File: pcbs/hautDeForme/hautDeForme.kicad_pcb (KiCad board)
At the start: 2 copper layers, 29.8 x 68.3 mm, 40 parts, among them J1 Conn_02x07_Counter_Clockwise, J6 USB4105-GF-A, U2 AZ1117CH-3.3TRG1, U4 CP2102N

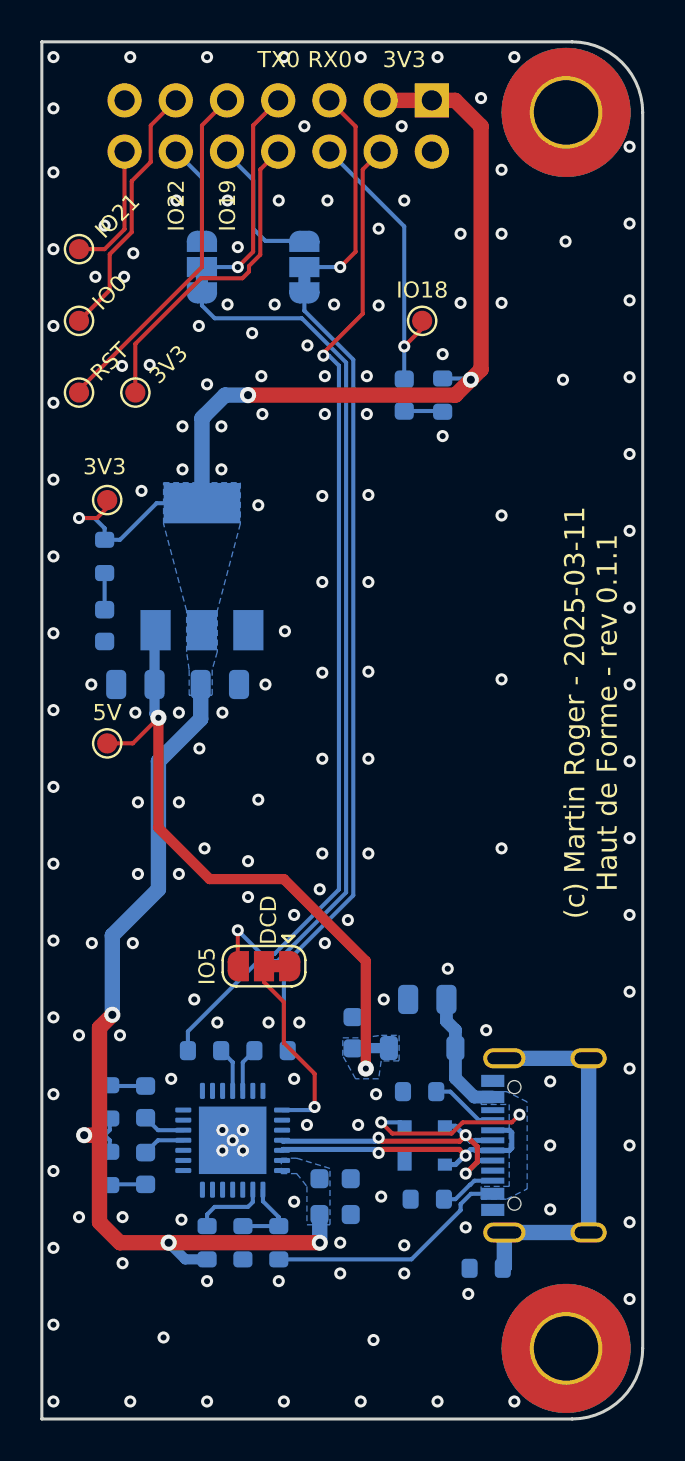
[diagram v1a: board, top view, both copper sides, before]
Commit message: Move to CP2102 non N
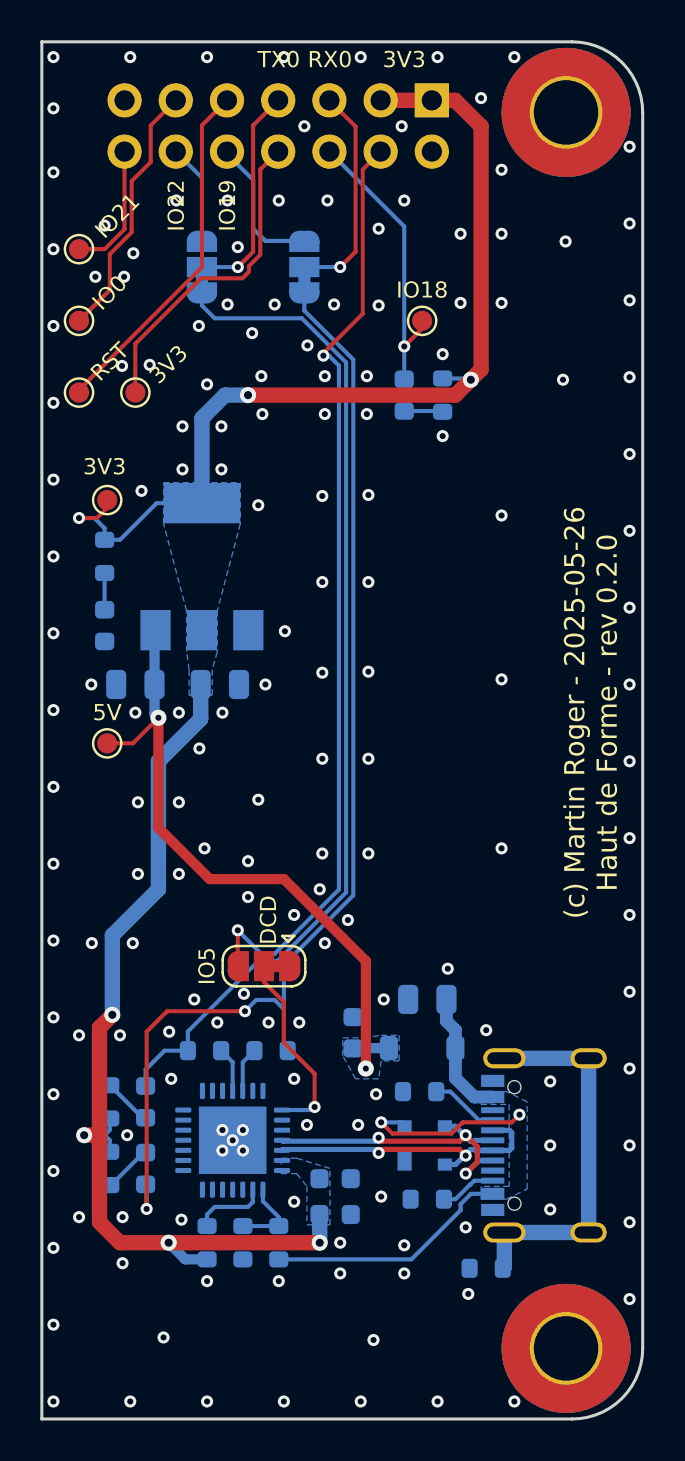
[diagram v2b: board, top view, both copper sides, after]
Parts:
- U4: value CP2102N -> CP2102-GM
- moved D11 3.30 mm to (126.0, 146.5)
- moved D9 3.30 mm to (126.0, 149.8)
- moved R34 3.30 mm to (124.2, 149.8), turned to -90 degrees
- moved R35 3.30 mm to (124.2, 146.5), turned to 90 degrees
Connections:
- D11 pad 1: Net-(D11-K) -> TX
- D9 pad 1: Net-(D9-K) -> RX
- U4 pad 18: Net-(D11-K) -> unconnected-(U4-~{RXT}/GPIO.1-Pad18)
- U4 pad 19: Net-(D9-K) -> unconnected-(U4-~{TXT}/GPIO.0-Pad19)
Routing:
- net RX: track 40.1 -> 57.7 mm, vias 0 -> 2
- net TX: track 46.9 -> 50.2 mm
- net Net-(D9-K): track 2.12 -> 0.00 mm
- net Net-(D11-K): track 2.12 -> 0.00 mm
- net Net-(D9-A): track 1.79 -> 2.45 mm
- net Net-(D11-A): track 1.79 -> 2.45 mm
- net GND: vias 164 -> 167
